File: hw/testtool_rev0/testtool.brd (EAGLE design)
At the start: 76.2 x 127 mm, 169 parts, among them IC1 SST26VF032BT-104I_SM, IC13 TLE9250XSJXUMA1, IC18 TLE9250XSJXUMA1, IC2 ATSAMV71Q21B-AABT, IC3 TJA1100HNZ, IC4 FT2232HL, J1 2305018-2, J2 2305018-2, J3 TBL009-254-04GY-2GY, J4 TBL009-254-04GY-2GY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

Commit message: Finish placing components for testtool
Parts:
- moved C21 182.3 mm to (45.7, 72.4), turned to 270 degrees
- moved C22 178.0 mm to (38.1, 72.4), turned to 90 degrees
- moved R193 174.9 mm to (67.3, 68.6)
- moved R188 168.3 mm to (67.3, 71.1)
- moved R88 165.2 mm to (71.1, 11.4)
- moved R12 163.1 mm to (58.4, 83.8), turned to 270 degrees
- moved R183 161.8 mm to (67.3, 73.7)
- moved R85 154.2 mm to (71.1, 24.1), turned to 90 degrees
- moved R87 149.1 mm to (58.4, 3.81), turned to 270 degrees
- moved C16 146.6 mm to (34.3, 116.8), turned to 90 degrees
- moved C5 146.6 mm to (43.2, 88.9), turned to 270 degrees
- moved C4 143.7 mm to (45.7, 94.0), turned to 90 degrees
- moved R86 141.7 mm to (58.4, 7.62), turned to 90 degrees
- moved R10 139.4 mm to (39.4, 80.0), turned to 180 degrees
- moved FL2 138.8 mm to (48.3, 94.0), turned to 270 degrees
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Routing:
- added copper zone on layer 2, net +3V3
- added copper zone on layer 1, net GND
- added copper zone on layer 15, net GND
- added copper zone on layer 16, net GND
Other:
- board size 76.2 x 127 mm -> 76.2 x 120.7 mm

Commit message: Finish laying out the test tool
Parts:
- moved R5 41.9 mm to (20.3, 87.6), turned to 90 degrees
- moved R6 41.9 mm to (22.9, 87.6), turned to 90 degrees
- moved R17 38.2 mm to (25.4, 88.9)
- moved R18 38.2 mm to (27.9, 88.9)
- moved R7 35.7 mm to (20.3, 91.4)
- moved R8 35.7 mm to (22.9, 91.4)
- moved R15 31.1 mm to (25.4, 85.1), turned to 90 degrees
- moved R16 31.1 mm to (27.9, 85.1), turned to 90 degrees
- moved R13 11.4 mm to (57.1, 73.7), turned to 90 degrees
- moved R14 11.4 mm to (59.7, 73.7), turned to 90 degrees
- moved R11 10.9 mm to (52.1, 73.7), turned to 90 degrees
- moved R12 10.9 mm to (54.6, 73.7), turned to 90 degrees
- moved C106 8.03 mm to (40.6, 21.6)
- moved C10 5.68 mm to (30.5, 95.2), turned to 90 degrees
- moved R26 5.68 mm to (45.7, 24.1)
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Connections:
- net +3V3: now also J6.2, J6.4
- net +5V: now also J6.6, J6.8
- net CAN0_H: now also J4.4; no longer J4.1
- net CAN0_L: now also J4.2; no longer J4.3
- net CAN1_H: now also J4.8; no longer J4.5
- net CAN1_L: now also J4.6; no longer J4.7
- net CON_ETH_TRX_M: now also J3.3; no longer J3.5
- net CON_ETH_TRX_P: now also J3.5; no longer J3.3
- net GND: now also J5.6, J5.8
- net JTAG_TCK: no longer TC1.7
- net SWITCHED_IGN: now also J5.4
- net VBATT: now also J5.2
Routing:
- net +3V3: track 0.00 -> 151.5 mm, vias 0 -> 38
- net +5V: track 0.00 -> 114.7 mm, vias 0 -> 4
- net INTREG_1V2: track 0.00 -> 105.1 mm
- net CAN1_RW_MODE: track 0.00 -> 72.2 mm, vias 0 -> 2
- net VUSB: track 0.00 -> 66.3 mm, vias 0 -> 2
- net HOST_USB_DM: track 0.00 -> 65.5 mm, vias 0 -> 3
- net CAN1_TX: track 0.00 -> 63.7 mm, vias 0 -> 2
- net HOST_USB_DP: track 0.00 -> 61.5 mm, vias 0 -> 2
- net CAN0_RW_MODE: track 0.00 -> 59.3 mm
- net RMII_RXER: track 0.00 -> 51.1 mm, vias 0 -> 2
- net RMII_RXD0: track 0.00 -> 49.9 mm, vias 0 -> 2
- net HOST_RESET: track 0.00 -> 49.3 mm, vias 0 -> 4
- net RMII_CRSDV: track 0.00 -> 47.2 mm, vias 0 -> 2
- net UART0_TXD: track 0.00 -> 47.2 mm
- net RMII_RXD1: track 0.00 -> 46.3 mm, vias 0 -> 2
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
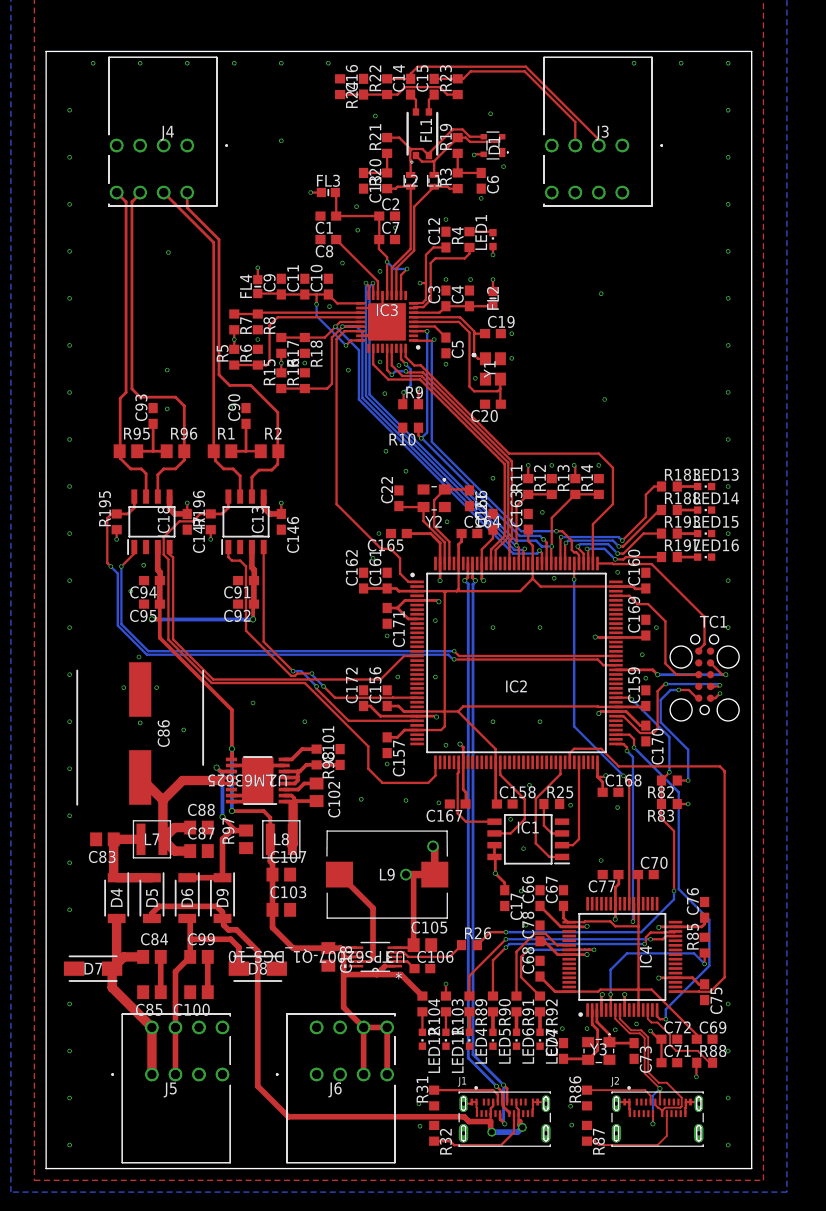
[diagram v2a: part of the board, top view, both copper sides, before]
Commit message: Fix silkscreen
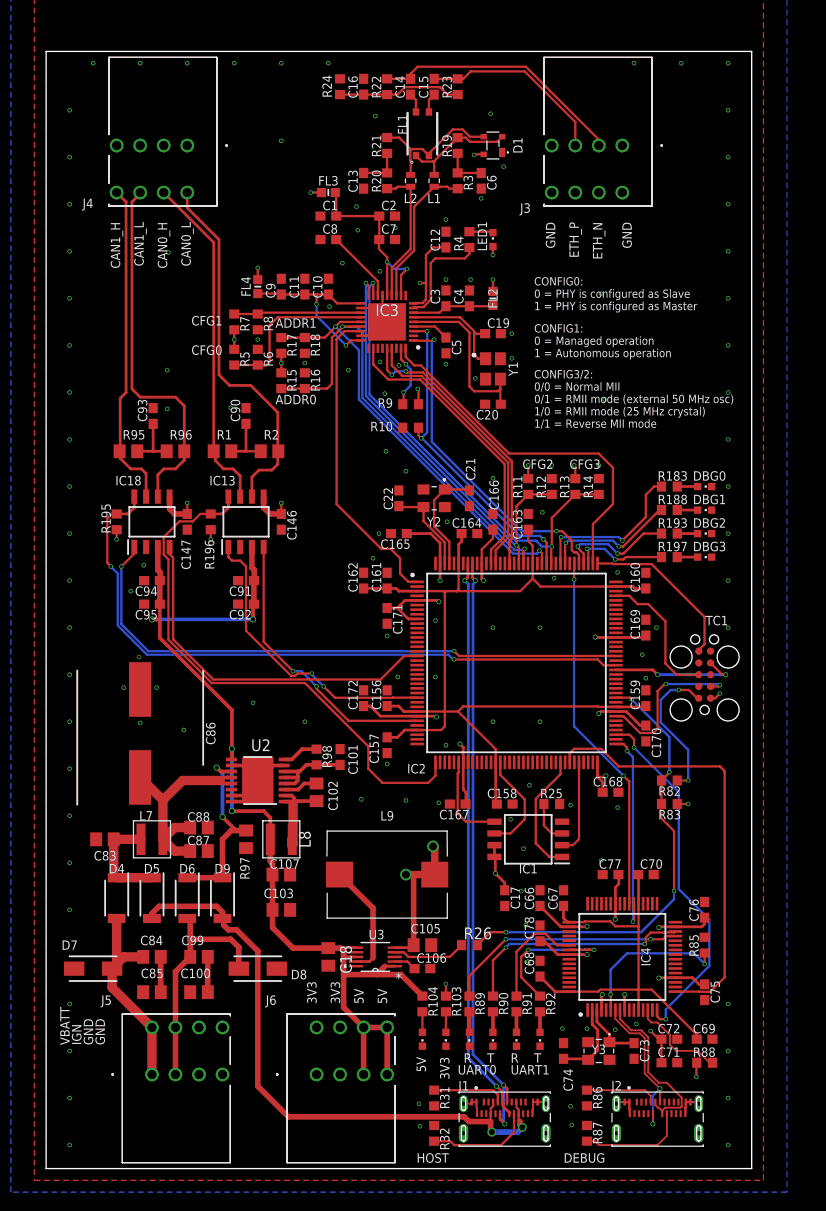
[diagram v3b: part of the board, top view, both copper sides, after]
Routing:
- net +3V3: track 151.5 -> 151.0 mm
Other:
- board text added: "3V3"
- board text added: "5V"
- board text added: "ADDR0"
- board text added: "ADDR1"
- board text added: "CAN0_H"
- board text added: "CAN0_L"
- board text added: "CAN1_H"
- board text added: "CAN1_L"
- board text added: "CFG0"
- board text added: "CFG1"
- board text added: "CFG2"
- board text added: "CFG3"
- board text added: "CONFIG0: 0 = PHY is configured as Slave 1 = PHY is configured as Master"
- board text added: "CONFIG1: 0 = Managed operation 1 = Autonomous operation"
- board text added: "CONFIG3/2: 0/0 = Normal MII 0/1 = RMII mode (external 50 MHz osc) 1/0 = RMII mode (25 MHz crystal) 1/1 = Reverse MII mode"
- board text added: "DBG0"
- board text added: "DBG1"
- board text added: "DBG2"
- board text added: "DBG3"
- board text added: "DEBUG"
- board text added: "ETH_N"
- board text added: "ETH_P"
- board text added: "GND"
- board text added: "HOST"
- board text added: "IGN"
- board text added: "R"
- board text added: "T"
- board text added: "UART0"
- board text added: "UART1"
- board text added: "VBATT"
